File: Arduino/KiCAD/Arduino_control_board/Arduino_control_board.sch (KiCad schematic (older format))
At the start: 21 parts, among them J1 Buttons 0, J2 Buttons 1

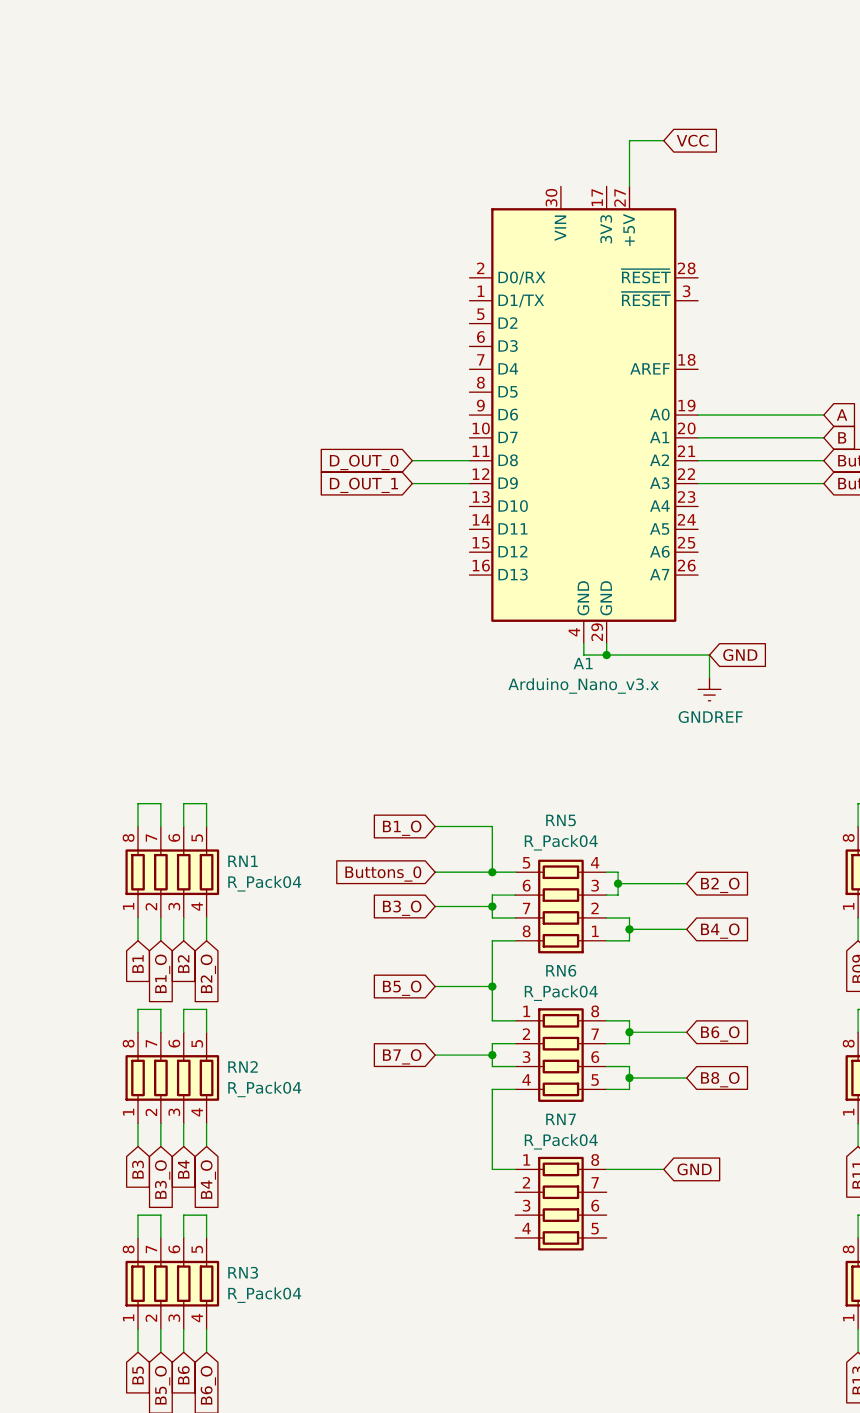
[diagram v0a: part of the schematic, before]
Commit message: add mode switches to schematic
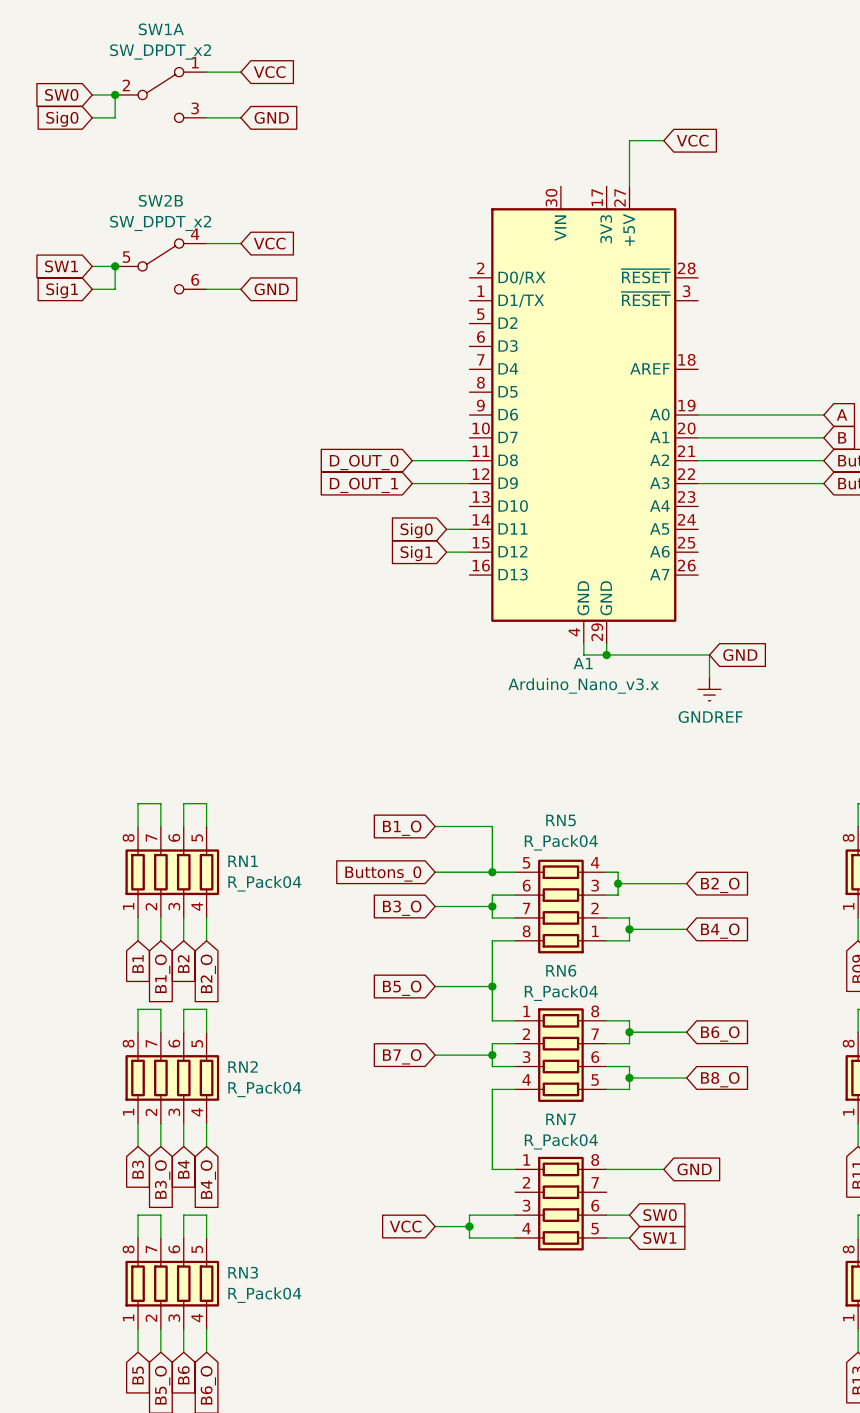
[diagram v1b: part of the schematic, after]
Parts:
- added SW1, SW2: SW_DPDT_x2, symbol Switch:SW_DPDT_x2
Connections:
- net GNDREF: now also SW1.3 (C), SW2.6 (C)
- net VCC: now also RN7.3 (R3.1), RN7.4 (R4.1), SW1.1 (A), SW2.4 (A)
- net SW0: now reaches A1.14 (D11)
- net SW0: now also RN7.6 (R3.2), SW1.2 (B)
- net SW1: now reaches A1.15 (D12)
- net SW1: now also RN7.5 (R4.2), SW2.5 (B)
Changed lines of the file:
@@
 	1    0    0    -1
 $EndComp
+$Comp
+L Switch:SW_DPDT_x2 SW1
+U 1 1 5EFB3E73
+P 1100 900
+F 0 "SW1" H 1100 1185 50  0000 C CNN
+F 1 "SW_DPDT_x2" H 1100 1094 50  0000 C CNN
+F 2 "" H 1100 900 50  0001 C CNN
+F 3 "~" H 1100 900 50  0001 C CNN
+	1    1100 900
+	1    0    0    -1
+$EndComp
+$Comp
+L Switch:SW_DPDT_x2 SW2
+U 2 1 5EFB4C19
+P 1100 1650
+F 0 "SW2" H 1100 1935 50  0000 C CNN
+F 1 "SW_DPDT_x2" H 1100 1844 50  0000 C CNN
+F 2 "" H 1100 1650 50  0001 C CNN
+F 3 "~" H 1100 1650 50  0001 C CNN
+	2    1100 1650
+	1    0    0    -1
+$EndComp
+Text GLabel 2300 5850 0    50   Input ~ 0
+VCC
+Wire Wire Line
+	2300 5850 2450 5850
+Wire Wire Line
+	2650 5800 2450 5800
+Wire Wire Line
+	2450 5800 2450 5850
+Wire Wire Line
+	2450 5900 2650 5900
+Connection ~ 2450 5850
+Wire Wire Line
+	2450 5850 2450 5900
+Text GLabel 3150 5800 2    50   Input ~ 0
+SW0
+Wire Wire Line
+	3150 5800 3050 5800
+Text GLabel 3150 5900 2    50   Input ~ 0
+SW1
+Wire Wire Line
+	3150 5900 3050 5900
+Text GLabel 800  900  0    50   Input ~ 0
+SW0
+Wire Wire Line
+	800  900  900  900
+Text GLabel 800  1650 0    50   Input ~ 0
+SW1
+Wire Wire Line
+	800  1650 900  1650
+Text GLabel 800  1000 0    50   Input ~ 0
+Sig0
+Wire Wire Line
+	800  1000 900  1000
+Text GLabel 800  1750 0    50   Input ~ 0
+Sig1
+Wire Wire Line
+	800  1750 900  1750
+Text GLabel 2350 2900 0    50   Input ~ 0
+Sig1
+Wire Wire Line
+	2350 2900 2450 2900
+Text GLabel 2350 2800 0    50   Input ~ 0
+Sig0
+Wire Wire Line
+	2350 2800 2450 2800
+Text GLabel 1450 1550 2    50   Input ~ 0
+VCC
+Wire Wire Line
+	1450 1550 1300 1550
+Text GLabel 1450 800  2    50   Input ~ 0
+VCC
+Wire Wire Line
+	1450 800  1300 800
+Wire Wire Line
+	900  900  900  1000
+Connection ~ 900  900
+Wire Wire Line
+	900  1750 900  1650
+Connection ~ 900  1650
+Text GLabel 1450 1000 2    50   Input ~ 0
+GND
+Wire Wire Line
+	1450 1000 1300 1000
+Text GLabel 1450 1750 2    50   Input ~ 0
+GND
+Wire Wire Line
+	1450 1750 1300 1750
 $EndSCHEMATC

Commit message: finsihed basic idea of arduino board. TODO: layout
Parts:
- H1, H2, H3, H4: footprint (none) -> MountingHole:MountingHole_3.2mm_M3
- J1, J2: footprint (none) -> TerminalBlock_RND:TerminalBlock_RND_205-00297_1x12_P5.08mm_Horizontal
- RN1, RN10, RN11, RN12, RN13, RN14, RN2, RN3, RN4, RN5, RN6, RN7, RN8, RN9: footprint (none) -> Resistor_SMD:R_Array_Convex_4x0603
- SW1, SW2: footprint (none) -> JS202011SCQN:JS202011SCQN
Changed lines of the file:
@@
 F 0 "J1" H 10280 1442 50  0000 L CNN
 F 1 "Buttons 0" H 10280 1351 50  0000 L CNN
-F 2 "" H 10200 1450 50  0001 C CNN
+F 2 "TerminalBlock_RND:TerminalBlock_RND_205-00297_1x12_P5.08mm_Horizontal" H 10200 1450 50  0001 C CNN
 F 3 "~" H 10200 1450 50  0001 C CNN
 	1    10200 1450
@@
 F 0 "J2" H 10280 2842 50  0000 L CNN
 F 1 "Buttons 1" H 10280 2751 50  0000 L CNN
-F 2 "" H 10200 2850 50  0001 C CNN
+F 2 "TerminalBlock_RND:TerminalBlock_RND_205-00297_1x12_P5.08mm_Horizontal" H 10200 2850 50  0001 C CNN
 F 3 "~" H 10200 2850 50  0001 C CNN
 	1    10200 2850
@@
 F 0 "RN1" H 1388 4346 50  0000 L CNN
 F 1 "R_Pack04" H 1388 4255 50  0000 L CNN
-F 2 "" V 1475 4300 50  0001 C CNN
+F 2 "Resistor_SMD:R_Array_Convex_4x0603" V 1475 4300 50  0001 C CNN
 F 3 "~" H 1200 4300 50  0001 C CNN
 	1    1200 4300
@@
 F 0 "RN5" V 3175 4400 50  0000 C CNN
 F 1 "R_Pack04" V 3084 4400 50  0000 C CNN
-F 2 "" V 3125 4400 50  0001 C CNN
+F 2 "Resistor_SMD:R_Array_Convex_4x0603" V 3125 4400 50  0001 C CNN
 F 3 "~" H 2850 4400 50  0001 C CNN
 	1    2850 4400
@@
 F 0 "RN6" V 2433 5150 50  0000 C CNN
 F 1 "R_Pack04" V 2524 5150 50  0000 C CNN
-F 2 "" V 3125 5150 50  0001 C CNN
+F 2 "Resistor_SMD:R_Array_Convex_4x0603" V 3125 5150 50  0001 C CNN
 F 3 "~" H 2850 5150 50  0001 C CNN
 	1    2850 5150
@@
 F 0 "RN2" H 1388 5246 50  0000 L CNN
 F 1 "R_Pack04" H 1388 5155 50  0000 L CNN
-F 2 "" V 1475 5200 50  0001 C CNN
+F 2 "Resistor_SMD:R_Array_Convex_4x0603" V 1475 5200 50  0001 C CNN
 F 3 "~" H 1200 5200 50  0001 C CNN
 	1    1200 5200
@@
 F 0 "RN3" H 1388 6146 50  0000 L CNN
 F 1 "R_Pack04" H 1388 6055 50  0000 L CNN
-F 2 "" V 1475 6100 50  0001 C CNN
+F 2 "Resistor_SMD:R_Array_Convex_4x0603" V 1475 6100 50  0001 C CNN
 F 3 "~" H 1200 6100 50  0001 C CNN
 	1    1200 6100
@@
 F 0 "RN4" H 1388 7046 50  0000 L CNN
 F 1 "R_Pack04" H 1388 6955 50  0000 L CNN
-F 2 "" V 1475 7000 50  0001 C CNN
+F 2 "Resistor_SMD:R_Array_Convex_4x0603" V 1475 7000 50  0001 C CNN
 F 3 "~" H 1200 7000 50  0001 C CNN
 	1    1200 7000
@@
 F 0 "RN7" V 2433 5800 50  0000 C CNN
 F 1 "R_Pack04" V 2524 5800 50  0000 C CNN
-F 2 "" V 3125 5800 50  0001 C CNN
+F 2 "Resistor_SMD:R_Array_Convex_4x0603" V 3125 5800 50  0001 C CNN
 F 3 "~" H 2850 5800 50  0001 C CNN
 	1    2850 5800
@@
 F 0 "RN8" H 4538 4346 50  0000 L CNN
 F 1 "R_Pack04" H 4538 4255 50  0000 L CNN
-F 2 "" V 4625 4300 50  0001 C CNN
+F 2 "Resistor_SMD:R_Array_Convex_4x0603" V 4625 4300 50  0001 C CNN
 F 3 "~" H 4350 4300 50  0001 C CNN
 	1    4350 4300
@@
 F 0 "RN12" V 6325 4400 50  0000 C CNN
 F 1 "R_Pack04" V 6234 4400 50  0000 C CNN
-F 2 "" V 6275 4400 50  0001 C CNN
+F 2 "Resistor_SMD:R_Array_Convex_4x0603" V 6275 4400 50  0001 C CNN
 F 3 "~" H 6000 4400 50  0001 C CNN
 	1    6000 4400
@@
 F 0 "RN13" V 5583 5150 50  0000 C CNN
 F 1 "R_Pack04" V 5674 5150 50  0000 C CNN
-F 2 "" V 6275 5150 50  0001 C CNN
+F 2 "Resistor_SMD:R_Array_Convex_4x0603" V 6275 5150 50  0001 C CNN
 F 3 "~" H 6000 5150 50  0001 C CNN
 	1    6000 5150
@@
 F 0 "RN9" H 4538 5246 50  0000 L CNN
 F 1 "R_Pack04" H 4538 5155 50  0000 L CNN
-F 2 "" V 4625 5200 50  0001 C CNN
+F 2 "Resistor_SMD:R_Array_Convex_4x0603" V 4625 5200 50  0001 C CNN
 F 3 "~" H 4350 5200 50  0001 C CNN
 	1    4350 5200
@@
 F 0 "RN10" H 4538 6146 50  0000 L CNN
 F 1 "R_Pack04" H 4538 6055 50  0000 L CNN
-F 2 "" V 4625 6100 50  0001 C CNN
+F 2 "Resistor_SMD:R_Array_Convex_4x0603" V 4625 6100 50  0001 C CNN
 F 3 "~" H 4350 6100 50  0001 C CNN
 	1    4350 6100
@@
 F 0 "RN11" H 4538 7046 50  0000 L CNN
 F 1 "R_Pack04" H 4538 6955 50  0000 L CNN
-F 2 "" V 4625 7000 50  0001 C CNN
+F 2 "Resistor_SMD:R_Array_Convex_4x0603" V 4625 7000 50  0001 C CNN
 F 3 "~" H 4350 7000 50  0001 C CNN
 	1    4350 7000
@@
 F 0 "RN14" V 5583 5800 50  0000 C CNN
 F 1 "R_Pack04" V 5674 5800 50  0000 C CNN
-F 2 "" V 6275 5800 50  0001 C CNN
+F 2 "Resistor_SMD:R_Array_Convex_4x0603" V 6275 5800 50  0001 C CNN
 F 3 "~" H 6000 5800 50  0001 C CNN
 	1    6000 5800
@@
 F 0 "H1" H 6000 1546 50  0000 L CNN
 F 1 "MountingHole" H 6000 1455 50  0000 L CNN
-F 2 "" H 5900 1500 50  0001 C CNN
+F 2 "MountingHole:MountingHole_3.2mm_M3" H 5900 1500 50  0001 C CNN
 F 3 "~" H 5900 1500 50  0001 C CNN
 	1    5900 1500
@@
 F 0 "H3" H 6750 1546 50  0000 L CNN
 F 1 "MountingHole" H 6750 1455 50  0000 L CNN
-F 2 "" H 6650 1500 50  0001 C CNN
+F 2 "MountingHole:MountingHole_3.2mm_M3" H 6650 1500 50  0001 C CNN
 F 3 "~" H 6650 1500 50  0001 C CNN
 	1    6650 1500
@@
 F 0 "H2" H 6000 1796 50  0000 L CNN
 F 1 "MountingHole" H 6000 1705 50  0000 L CNN
-F 2 "" H 5900 1750 50  0001 C CNN
+F 2 "MountingHole:MountingHole_3.2mm_M3" H 5900 1750 50  0001 C CNN
 F 3 "~" H 5900 1750 50  0001 C CNN
 	1    5900 1750
@@
 F 0 "H4" H 6750 1796 50  0000 L CNN
 F 1 "MountingHole" H 6750 1705 50  0000 L CNN
-F 2 "" H 6650 1750 50  0001 C CNN
+F 2 "MountingHole:MountingHole_3.2mm_M3" H 6650 1750 50  0001 C CNN
 F 3 "~" H 6650 1750 50  0001 C CNN
 	1    6650 1750
@@
 F 0 "SW1" H 1100 1185 50  0000 C CNN
 F 1 "SW_DPDT_x2" H 1100 1094 50  0000 C CNN
-F 2 "" H 1100 900 50  0001 C CNN
+F 2 "JS202011SCQN:JS202011SCQN" H 1100 900 50  0001 C CNN
 F 3 "~" H 1100 900 50  0001 C CNN
 	1    1100 900
@@
 F 0 "SW2" H 1100 1935 50  0000 C CNN
 F 1 "SW_DPDT_x2" H 1100 1844 50  0000 C CNN
-F 2 "" H 1100 1650 50  0001 C CNN
+F 2 "JS202011SCQN:JS202011SCQN" H 1100 1650 50  0001 C CNN
 F 3 "~" H 1100 1650 50  0001 C CNN
 	2    1100 1650

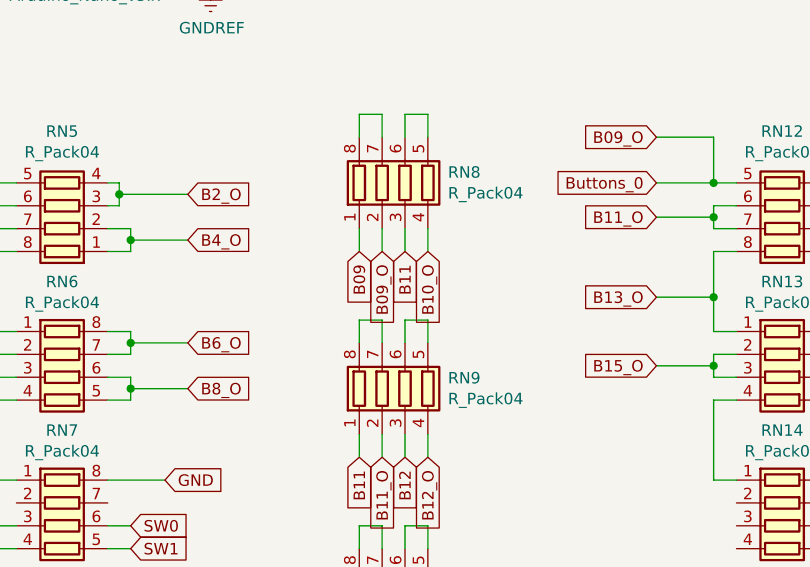
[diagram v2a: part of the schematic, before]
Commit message: 80% done with the controller. Will have done and ready for review this friday.
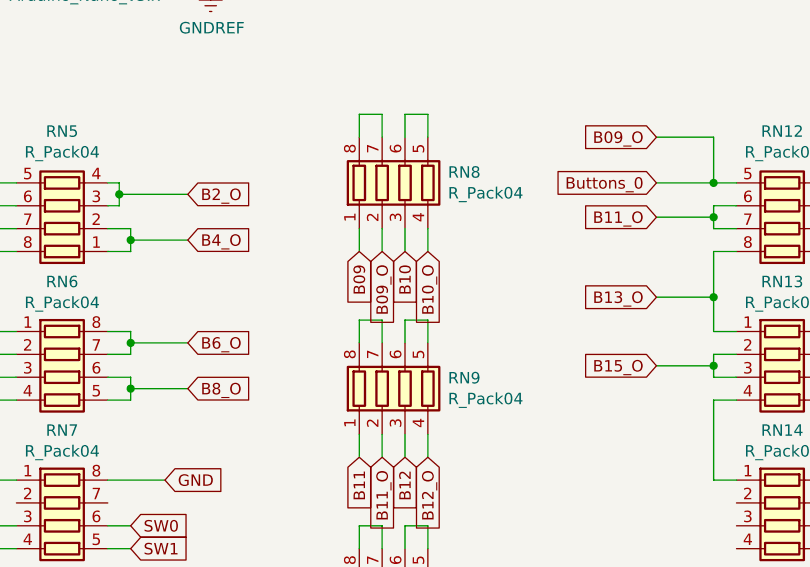
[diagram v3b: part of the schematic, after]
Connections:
- net B10: now also RN8.3 (R3.1)
- net B11: no longer RN8.3 (R3.1)
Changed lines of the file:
@@
 Buttons_0
 Text GLabel 4350 4600 3    50   Input ~ 0
-B11
+B10
 Wire Wire Line
 	4350 4600 4350 4500
